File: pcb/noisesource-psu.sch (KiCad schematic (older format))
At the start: 17 parts, among them U1 TLV61046ADB

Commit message: pcb: Continued initial schematic creation
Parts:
- added C1, C2: 47pF, symbol Device:C
- added FB1: Ferrite_Bead, symbol Device:Ferrite_Bead
- added J1: USB_B_Micro, symbol Connector:USB_B_Micro
- added R1, R2: 27, symbol Device:R
- gave numbers to parts that had none: 14
- renumbered C2 to C5, U1 to U4
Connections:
- net labels added: +3V3, PWREN#
- wire segments 57 -> 88
- no-connect marks 0 -> 4
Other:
- note added: "CBUS IO are 3.3V"
- moved on the sheet: C3, C4, C5, D1, D2, L1, R3, R4, R5, R6, R7, R8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

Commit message: pcb: Changed voltage regulator to TPS61175
The previous TLV61046 is not rated to handle the peak inductor
currents during startup.
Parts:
- removed D1, D2: D, symbol Device:D
- removed U2: INA138, Package_TO_SOT_SMD:SOT-23-5, symbol Amplifier_Current:INA138
- removed U3: LMV321, symbol Amplifier_Operational:LMV321
- removed U4: TLV61046ADB, Package_TO_SOT_SMD:SOT-23-6, symbol Regulator_Switching:TLV61046ADB
- added C6: 47nF, symbol Device:C
- added C7: 680pF, symbol Device:C
- added C8: 47uF, symbol Device:CP1
- added C9: 1uF, symbol Device:C
- added D1, D2: LED, Resistor_SMD:R_0603_1608Metric_Pad1.05x0.95mm_HandSolder, symbol Device:LED
- added D3: D, symbol Device:D
- added H1, H2, H3, H4: MountingHole, symbol Mechanical:MountingHole
- added J2: Conn_Coaxial, Connector_Coaxial:BNC_Amphenol_B6252HB-NPP3G-50_Horizontal, symbol Connector:Conn_Coaxial
- added U2: TPS22917DBV, Package_TO_SOT_SMD:SOT-23-6, symbol Power_Management:TPS22917DBV
- added U3: TPS61175, symbol tps61175:TPS61175
- C1, C2, C4, FB1, R1, R2, R4, R5: footprint (none) -> Resistor_SMD:R_0603_1608Metric_Pad1.05x0.95mm_HandSolder
- C3: value 0.1uF -> 10nF; footprint (none) -> Resistor_SMD:R_0603_1608Metric_Pad1.05x0.95mm_HandSolder
- C5: value C -> 10uF
- J1: footprint (none) -> Connector_USB:USB_Micro-AB_Molex_47590-0001
- L1: value L -> 27uF
- R3: value 0.5 -> R; footprint (none) -> Resistor_SMD:R_0603_1608Metric_Pad1.05x0.95mm_HandSolder
- R6: value R -> 86.6k
- R7: value R -> 28.7k
- R8: value R -> 357k
- R9: value R -> 16.2k
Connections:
- net labels added: Vout_EN
- net labels removed: +5V, Vout_en
- wire segments 88 -> 116
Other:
- note added: "! CBUS IO are 3.3V"
- note removed: "CBUS IO are 3.3V"
- note removed: "Pre-charger to reduce inrush current"
- note removed: "Vbus or V5V?\n"
- note removed: "Wrong OpAmp. Needs to be updated"
- moved on the sheet: C1, C2, FB1, J1, R1, R2, U1

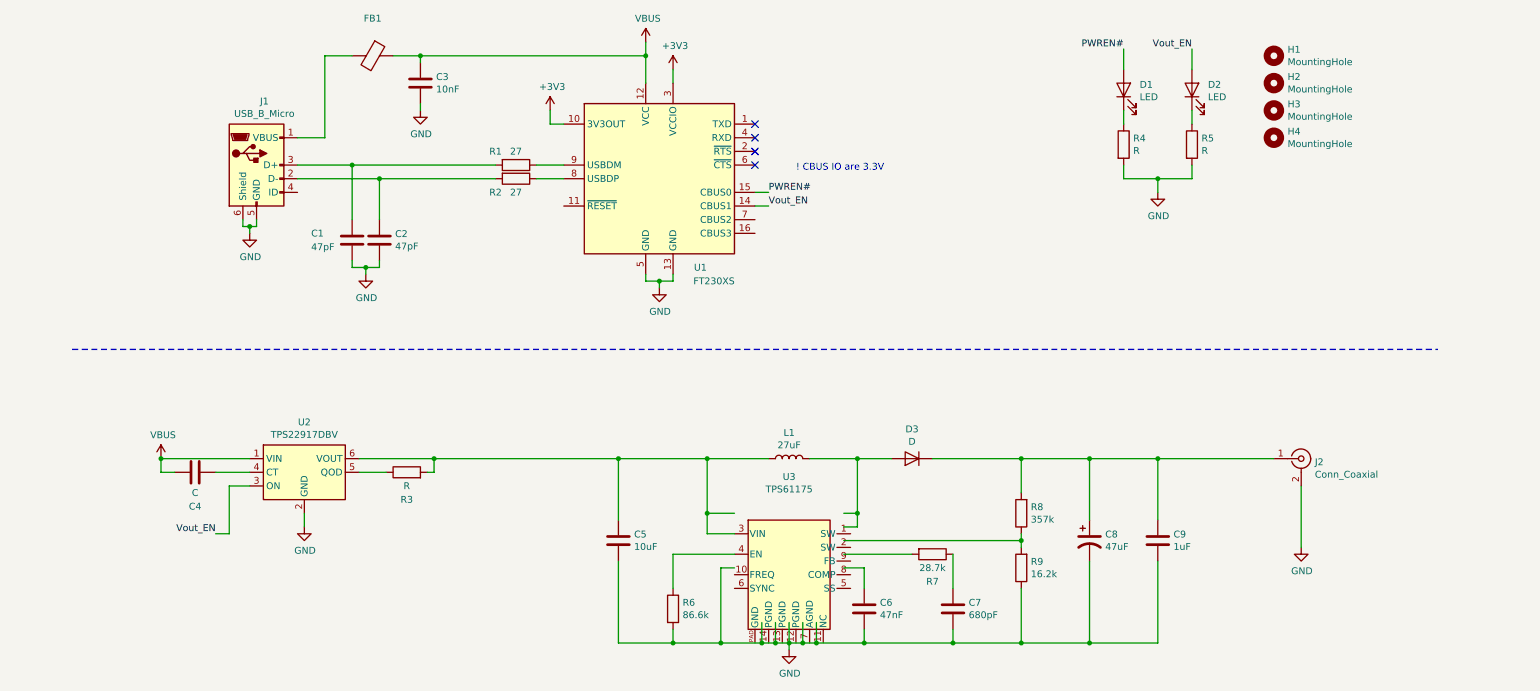
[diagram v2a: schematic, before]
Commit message: Updated schematic
Added PDF export
Added comments on output filter and output switch
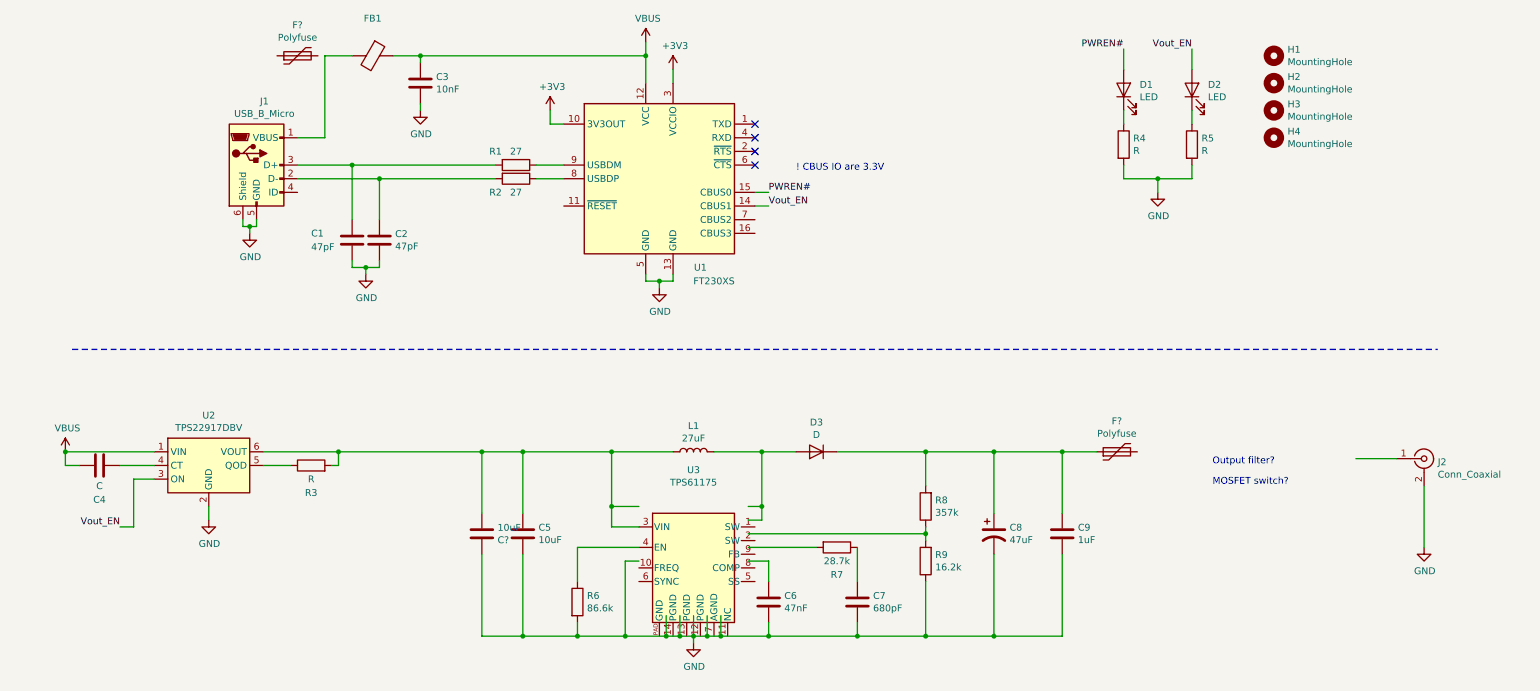
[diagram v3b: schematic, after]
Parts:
- added C?: 10uF, symbol Device:C
- added F? (x2): Polyfuse, symbol Device:Polyfuse
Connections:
- wire segments 116 -> 121
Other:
- note added: "MOSFET switch?"
- note added: "Output filter?"
- moved on the sheet: C4, C5, C6, C7, C8, C9, D3, J2, L1, R3, R6, R7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

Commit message: schematic: Added output filter, added footprints
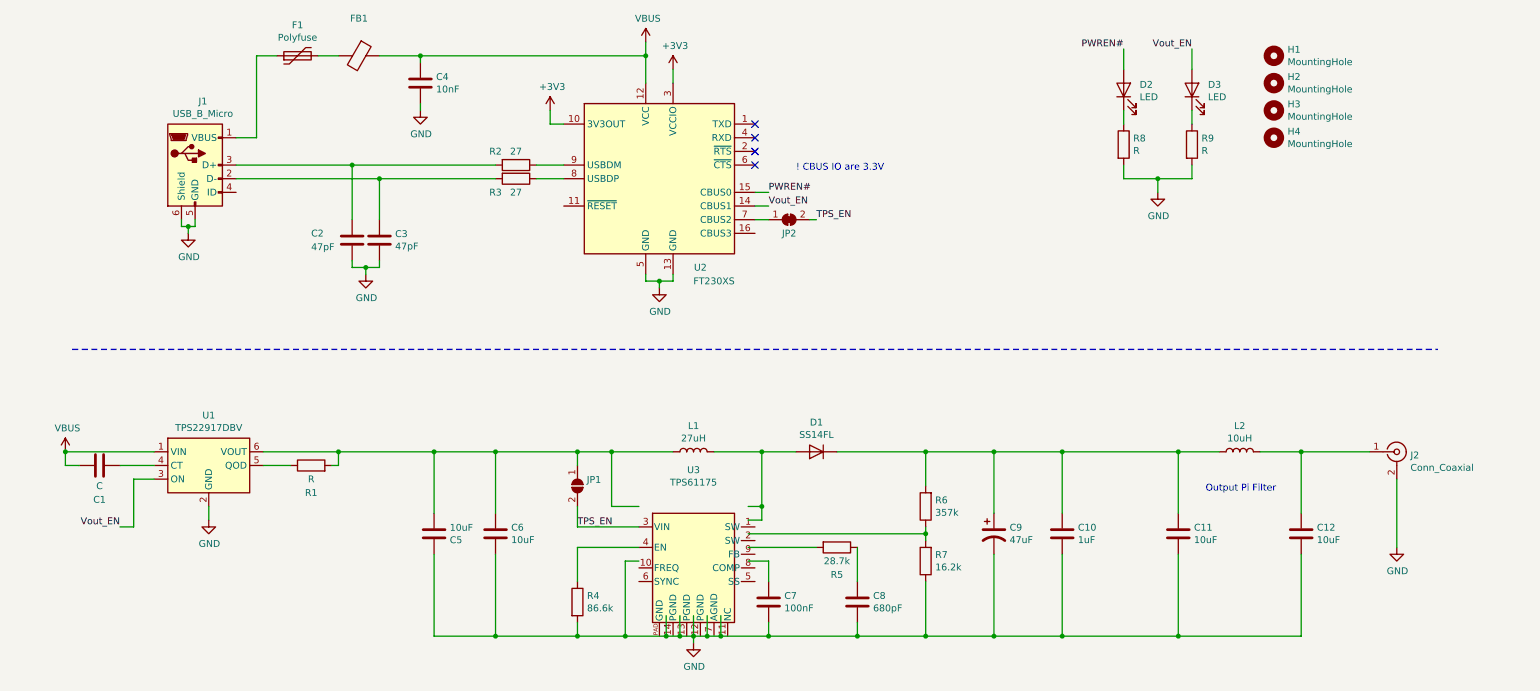
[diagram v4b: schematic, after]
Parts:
- removed F?: Polyfuse, symbol Device:Polyfuse
- added C11, C12: 10uF, Capacitor_SMD:C_0603_1608Metric_Pad1.05x0.95mm_HandSolder, symbol Device:C
- added JP1: SolderJumper_2_Open, symbol Jumper:SolderJumper_2_Open
- added JP2: SolderJumper_2_Bridged, symbol Jumper:SolderJumper_2_Bridged
- added L2: 10uH, symbol Device:L
- C1: renamed from C4; footprint Resistor_SMD:R_0603_1608Metric_Pad1.05x0.95mm_HandSolder -> Capacitor_SMD:C_0603_1608Metric_Pad1.05x0.95mm_HandSolder
- C10: renamed from C9; footprint (none) -> Capacitor_SMD:C_0603_1608Metric_Pad1.05x0.95mm_HandSolder
- C2: renamed from C1; footprint Resistor_SMD:R_0603_1608Metric_Pad1.05x0.95mm_HandSolder -> Capacitor_SMD:C_0603_1608Metric_Pad1.05x0.95mm_HandSolder
- C3: renamed from C2; footprint Resistor_SMD:R_0603_1608Metric_Pad1.05x0.95mm_HandSolder -> Capacitor_SMD:C_0603_1608Metric_Pad1.05x0.95mm_HandSolder
- C4: renamed from C3; footprint Resistor_SMD:R_0603_1608Metric_Pad1.05x0.95mm_HandSolder -> Capacitor_SMD:C_0603_1608Metric_Pad1.05x0.95mm_HandSolder
- C5: renamed from C?; footprint (none) -> Capacitor_SMD:C_0603_1608Metric_Pad1.05x0.95mm_HandSolder
- C6: renamed from C5; footprint (none) -> Capacitor_SMD:C_0603_1608Metric_Pad1.05x0.95mm_HandSolder
- C7: renamed from C6; value 47nF -> 100nF; footprint (none) -> Capacitor_SMD:C_0603_1608Metric_Pad1.05x0.95mm_HandSolder
- C8: renamed from C7; footprint (none) -> Capacitor_SMD:C_0603_1608Metric_Pad1.05x0.95mm_HandSolder
- C9: renamed from C8; footprint (none) -> Capacitor_SMD:C_Elec_8x6.2
- D1: renamed from D3; value D -> SS14FL; footprint (none) -> Diode_SMD:D_SOD-123F
- F1: renamed from F?; footprint (none) -> Fuse:Fuse_0805_2012Metric_Pad1.15x1.40mm_HandSolder
- H1, H2, H3, H4: footprint (none) -> MountingHole:MountingHole_3.2mm_M3
- L1: value 27uF -> 27uH
- R4: renamed from R6; footprint (none) -> Resistor_SMD:R_0603_1608Metric_Pad1.05x0.95mm_HandSolder
- R5: renamed from R7; footprint (none) -> Resistor_SMD:R_0603_1608Metric_Pad1.05x0.95mm_HandSolder
- R6: renamed from R8; footprint (none) -> Resistor_SMD:R_0603_1608Metric_Pad1.05x0.95mm_HandSolder
- R7: renamed from R9; footprint (none) -> Resistor_SMD:R_0603_1608Metric_Pad1.05x0.95mm_HandSolder
- renumbered D1 to D2, D2 to D3, R3 to R1, R1 to R2, R2 to R3, R4 to R8, R5 to R9, U2 to U1, U1 to U2
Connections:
- net labels added: TPS_EN
- wire segments 121 -> 134
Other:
- note added: "Output Pi Filter"
- note removed: "MOSFET switch?"
- note removed: "Output filter?"
- moved on the sheet: C5, C6, FB1, J1, J2

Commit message: pcb: Updated schematic and layout
Schematic:
  Added testpoints
  Added ground pad to TPS51175

Layout:
  Completed initial layout of PCB
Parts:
- added 28V1, 5V1, VBUS1: TestPoint, TestPoint:TestPoint_THTPad_1.0x1.0mm_Drill0.5mm, symbol Connector:TestPoint
- added D4: USBLC6-2SC6, digikey-footprints:SOT23-6L, symbol dk_TVS-Diodes:USBLC6-2SC6
- added U4: FT230XS, Package_SO:SSOP-16_3.9x4.9mm_P0.635mm, symbol Interface_USB:FT230XS
- C1: value C -> 100pF
- C2, C3: Digi-Key PN (none) -> 732-7764-1-ND; MPN (none) -> 885012006021
- C4: Digi-Key PN (none) -> 732-7959-1-ND; MPN (none) -> 885012206040
- C7: Digi-Key PN (none) -> 1276-1934-1-ND; MPN (none) -> CL10B104KB8NFNC
- C8: Digi-Key PN (none) -> 732-8000-1-ND; MPN (none) -> 885012206082
- C9: Digi-Key PN (none) -> 493-9586-1-ND; MPN (none) -> UUR1V470MCL6GS
- D1: Digi-Key PN (none) -> SS14FLCT-ND; MPN (none) -> SS14FL
- D2, D3: Digi-Key PN (none) -> 732-4980-1-ND; MPN (none) -> 150060VS75000
- F1: Digi-Key PN (none) -> F6725CT-ND; MPN (none) -> 0805L110WR
- FB1: Digi-Key PN (none) -> 587-1869-1-ND; MPN (none) -> BK1608HS220-T
- J1: Digi-Key PN (none) -> WM17144CT-ND; MPN (none) -> 0475900001
- JP1: footprint (none) -> Jumper:SolderJumper-2_P1.3mm_Open_Pad1.0x1.5mm
- JP2: footprint (none) -> Jumper:SolderJumper-2_P1.3mm_Bridged_Pad1.0x1.5mm
- L1: footprint (none) -> l_bourns-SRN5040:L_Bourns-SRN5040; Digi-Key PN (none) -> SRN5040-270MCT-ND; MPN (none) -> SRN5040-270M
- L2: footprint (none) -> l_bourns-SRN5040:L_Bourns-SRN5040; Digi-Key PN (none) -> SRN5040-100MCT-ND; MPN (none) -> SRN5040-100M
- R2, R3: Digi-Key PN (none) -> 2019-RK73B1JTTD270JCT-ND; MPN (none) -> RK73B1JTTD270J
- R8, R9: value R -> 330; Digi-Key PN (none) -> 2019-RK73B1JTTD331JCT-ND; MPN (none) -> RK73B1JTTD331J
- U2: Digi-Key PN (none) -> 768-1135-1-ND; MPN (none) -> FT230XS-R
- U3: footprint (none) -> tssop14:TSSOP14; Digi-Key PN (none) -> 296-24013-1-ND; MPN (none) -> TPS61175PWPR
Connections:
- wire segments 134 -> 152
- no-connect marks 4 -> 5
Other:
- moved on the sheet: C2, C3, C4, F1, FB1, J1, U3

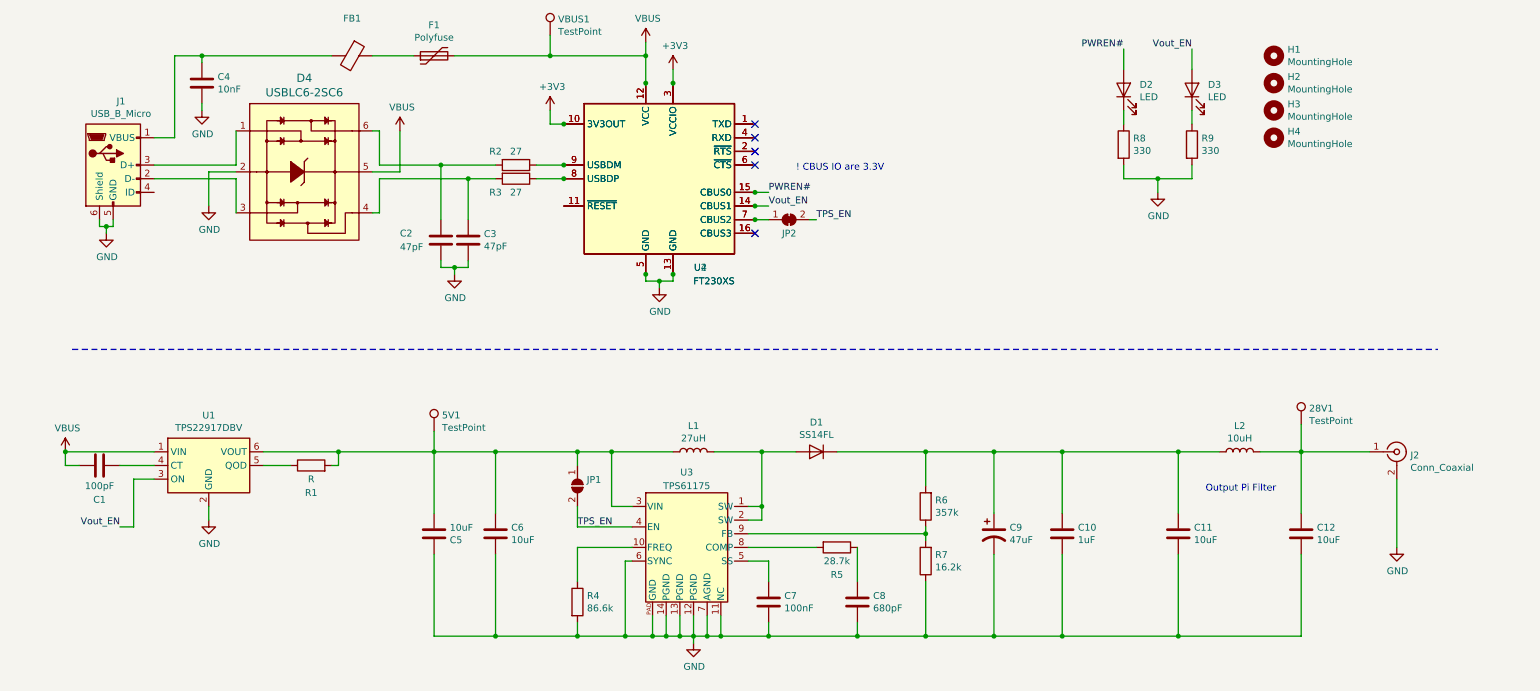
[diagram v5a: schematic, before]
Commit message: pcb: Updated schematic and layout
Added 3.3v decoupling cap
Added top ground fill
Changed solder jumper footprint
Added sense and test load resistors
Changed SMPS ground pad to thermal fill
Changed mounting holes to plated through vias with pads
Moved test points
Misc rerouting
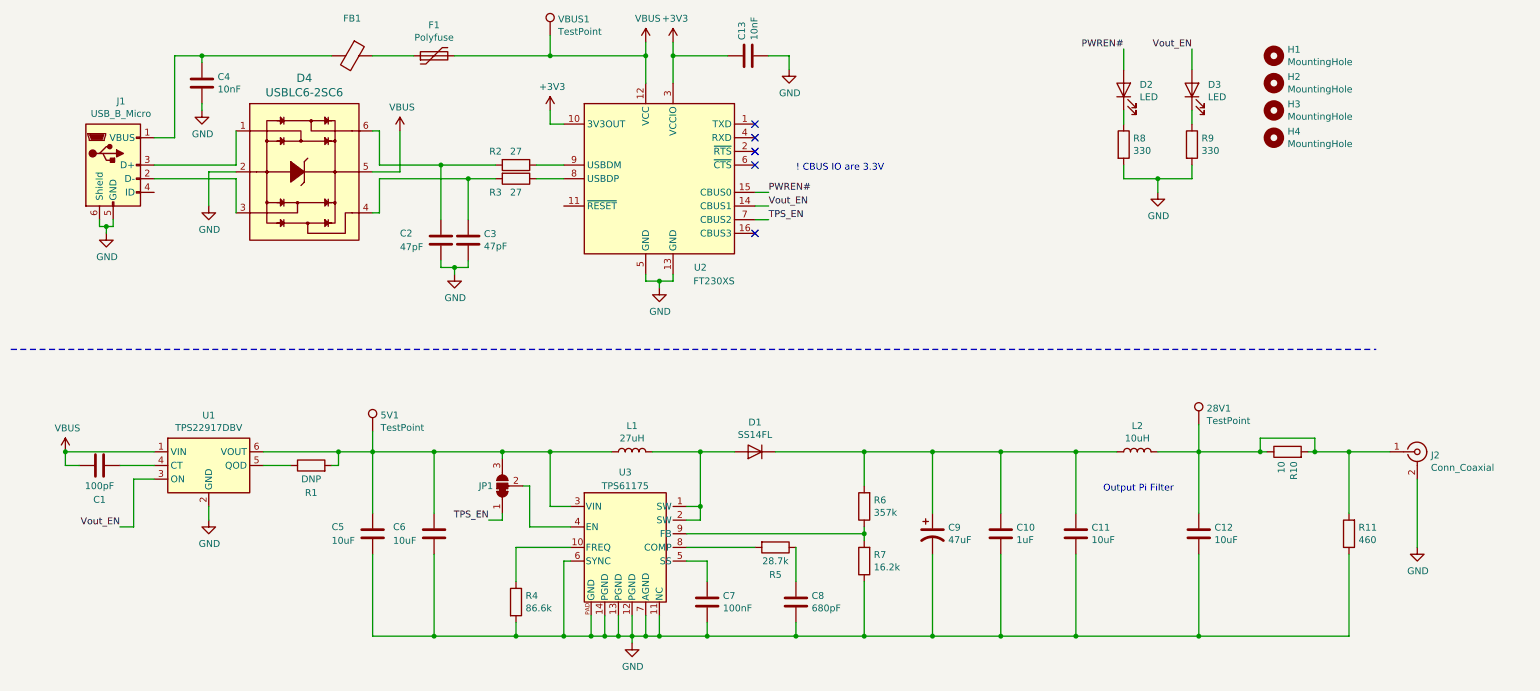
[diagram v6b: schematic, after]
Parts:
- removed JP1: SolderJumper_2_Open, Jumper:SolderJumper-2_P1.3mm_Open_Pad1.0x1.5mm, symbol Jumper:SolderJumper_2_Open
- removed JP2: SolderJumper_2_Bridged, Jumper:SolderJumper-2_P1.3mm_Bridged_Pad1.0x1.5mm, symbol Jumper:SolderJumper_2_Bridged
- removed U4: FT230XS, Package_SO:SSOP-16_3.9x4.9mm_P0.635mm, symbol Interface_USB:FT230XS
- added C13: 10nF, Capacitor_SMD:C_0603_1608Metric_Pad1.05x0.95mm_HandSolder, symbol Device:C
- added JP1: SolderJumper_3_Bridged12, Jumper:SolderJumper-3_P1.3mm_Bridged12_RoundedPad1.0x1.5mm, symbol Jumper:SolderJumper_3_Bridged12
- added R10: 10, Resistor_SMD:R_0402_1005Metric, symbol Device:R
- added R11: 460, Resistor_SMD:R_2010_5025Metric_Pad1.52x2.65mm_HandSolder, symbol Device:R
- C1: Digi-Key PN (none) -> 732-7922-1-ND; MPN (none) -> 885012206003
- C10: Digi-Key PN (none) -> 587-2400-1-ND; MPN (none) -> UMK107BJ105KA-T
- C11, C12, C5, C6: Digi-Key PN (none) -> 490-13248-1-ND; MPN (none) -> GRM188R6YA106MA73D
- D4: Digi-Key PN (none) -> 497-5235-1-ND; Digi-Key_PN 497-5235-1-ND -> (none)
- H1, H2, H3, H4: footprint MountingHole:MountingHole_3.2mm_M3 -> MountingHole:MountingHole_3.2mm_M3_Pad_Via
- J2: MPN (none) -> B6252HB-NPP3G-50
- R1: value R -> DNP
- R4: Digi-Key PN (none) -> 2019-RK73H1JTTD8662FCT-ND; MPN (none) -> RK73H1JTTD8662F
- R5: Digi-Key PN (none) -> 2019-RK73H1JTTD2872FCT-ND; MPN (none) -> RK73H1JTTD2872F
- R6: Digi-Key PN (none) -> 2019-RK73H1JTTD3573FCT-ND; MPN (none) -> RK73H1JTTD3573F
- R7: Digi-Key PN (none) -> 2019-RK73H1JTTD1622FCT-ND; MPN (none) -> RK73H1JTTD1622F
- U1: Digi-Key PN (none) -> 296-50498-1-ND; MPN (none) -> TPS22917DBVR
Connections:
- net +3V3: now also C13.1
- net GND: now also C13.2, R11.1
- net TPS_EN: now also U2.7 (CBUS2), JP1.1 (A); no longer U3.4 (EN)
- net at 5V1.1, C5.2, C6.1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: now also JP1.3 (B)
- net at 28V1.1, C12.1, J2.1 (In)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: now also R10.1, R10.2, R11.2
- new net: JP1.2 (C), U3.4 (EN)
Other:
- moved on the sheet: 28V1, 5V1, C10, C11, C12, C5, C6, C7, C8, C9, D1, J2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
